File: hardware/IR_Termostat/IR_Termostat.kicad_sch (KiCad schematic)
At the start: 7 parts, among them J1 USB_C_Receptacle_PowerOnly_6P, J2 Conn_01x02_Socket, Q1 PMOS, U1 TP4056-42-ESOP8

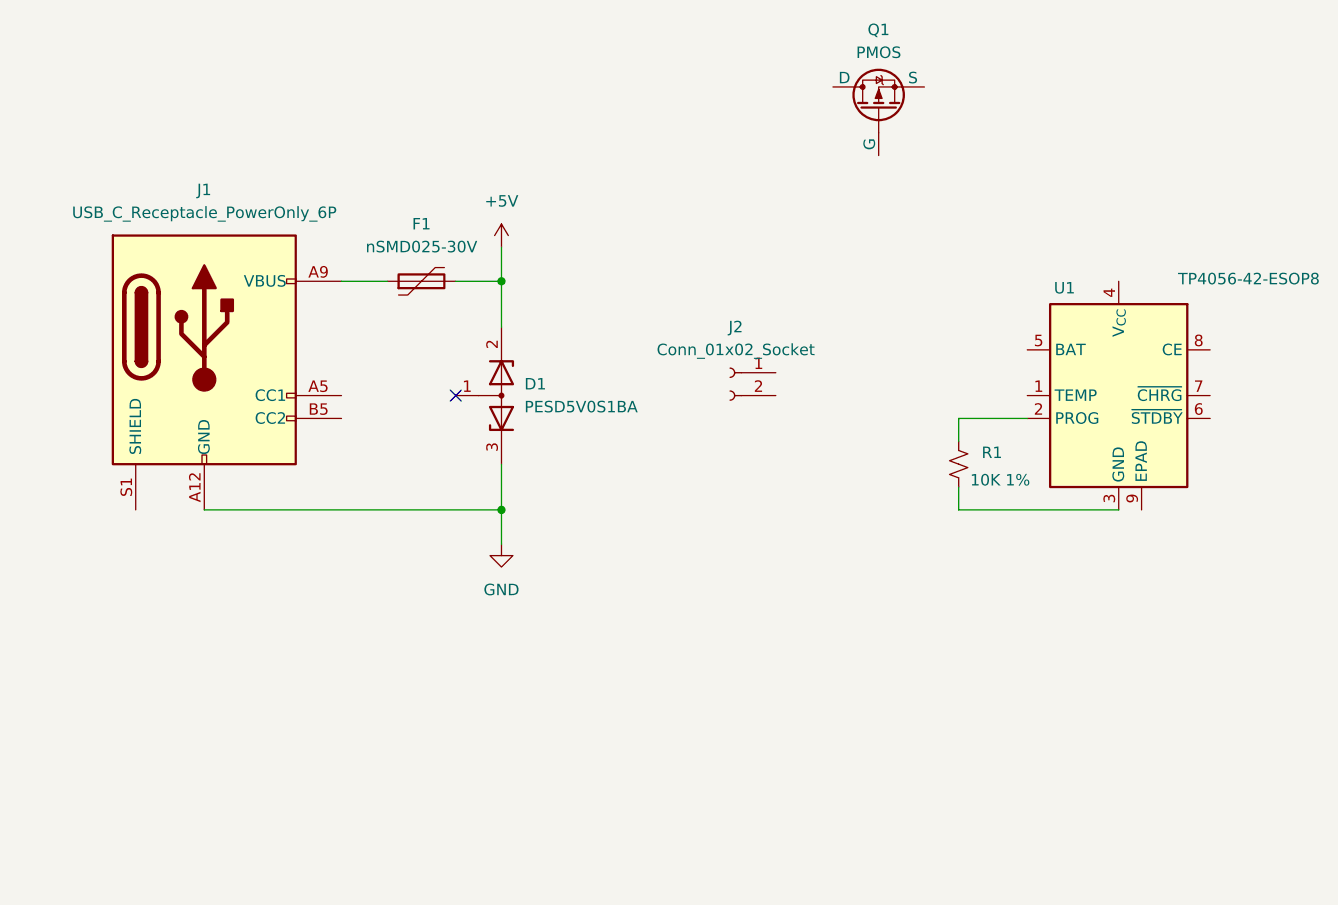
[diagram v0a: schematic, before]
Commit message: Feat: NTC improved
Also added CC1 and CC2 Resistors and a text box explaining the eletrical tolerances
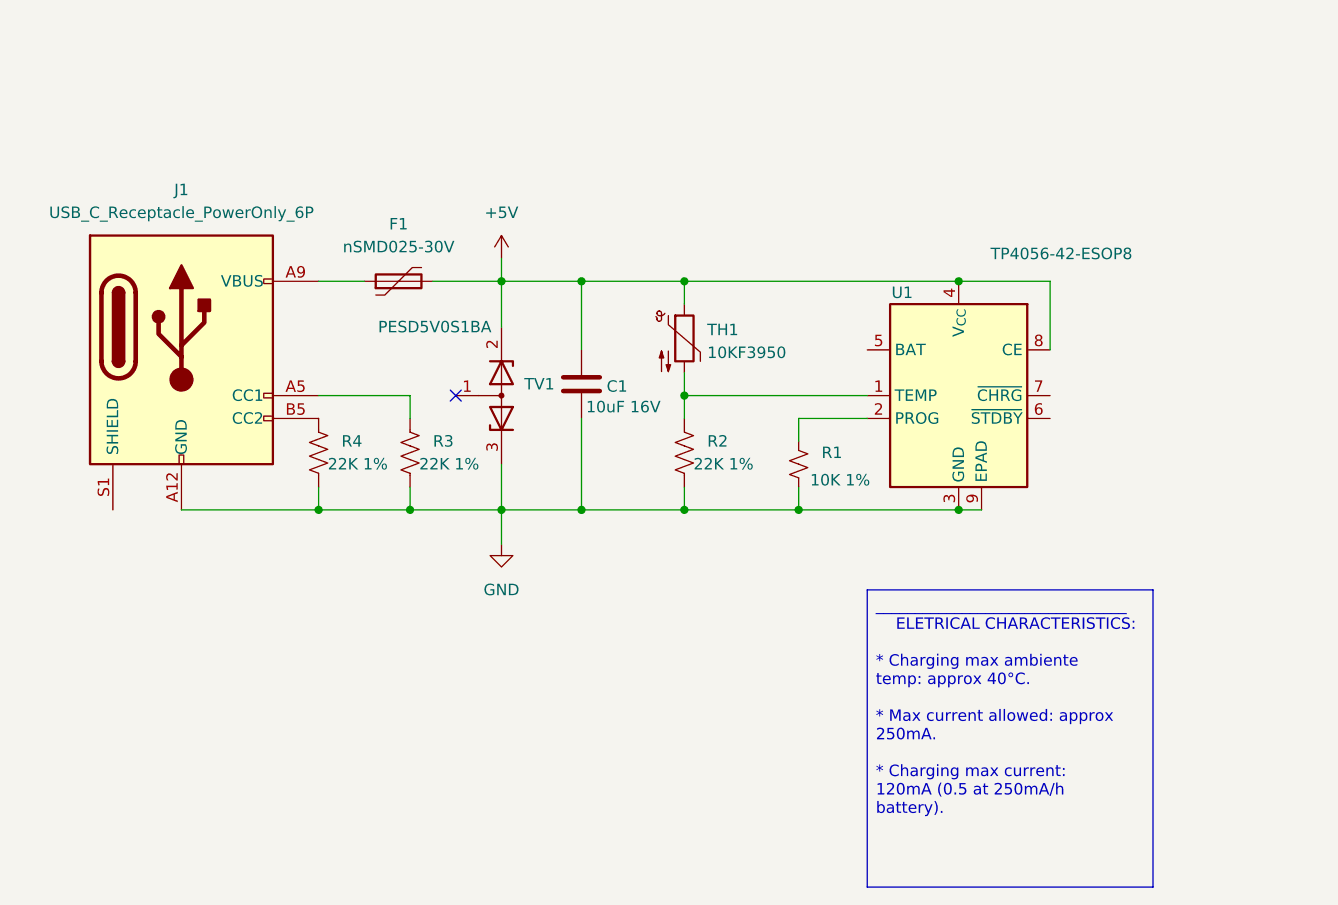
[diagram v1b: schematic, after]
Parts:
- removed J2: Conn_01x02_Socket, Connector:JWT_A3963_1x02_P3.96mm_Vertical, symbol Connector:Conn_01x02_Socket
- removed Q1: PMOS, symbol Simulation_SPICE:PMOS
- added C1: 10uF 16V, Capacitor_SMD:C_0805_2012Metric_Pad1.18x1.45mm_HandSolder, symbol Device:C
- added R2, R3, R4: 22K 1%, Resistor_SMD:R_0805_2012Metric_Pad1.20x1.40mm_HandSolder, symbol Device:R_US
- added TH1: 10KF3950, Resistor_SMD:R_0805_2012Metric_Pad1.20x1.40mm_HandSolder, symbol Device:Thermistor_NTC
- renumbered D1 to TV1
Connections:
- net +5V: now also U1.4 (V_{CC}), U1.8 (CE), C1.1, TH1.1
- net GND: now also R1.2, U1.3 (GND), U1.9 (EPAD), C1.2, R2.2, R3.2, R4.2
- net at U1.1 (TEMP): now also R2.1, TH1.2
- net at J1.A5 (CC1): now also R3.1
- net at J1.B5 (CC2): now also R4.1
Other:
- moved on the sheet: F1, J1, R1, U1

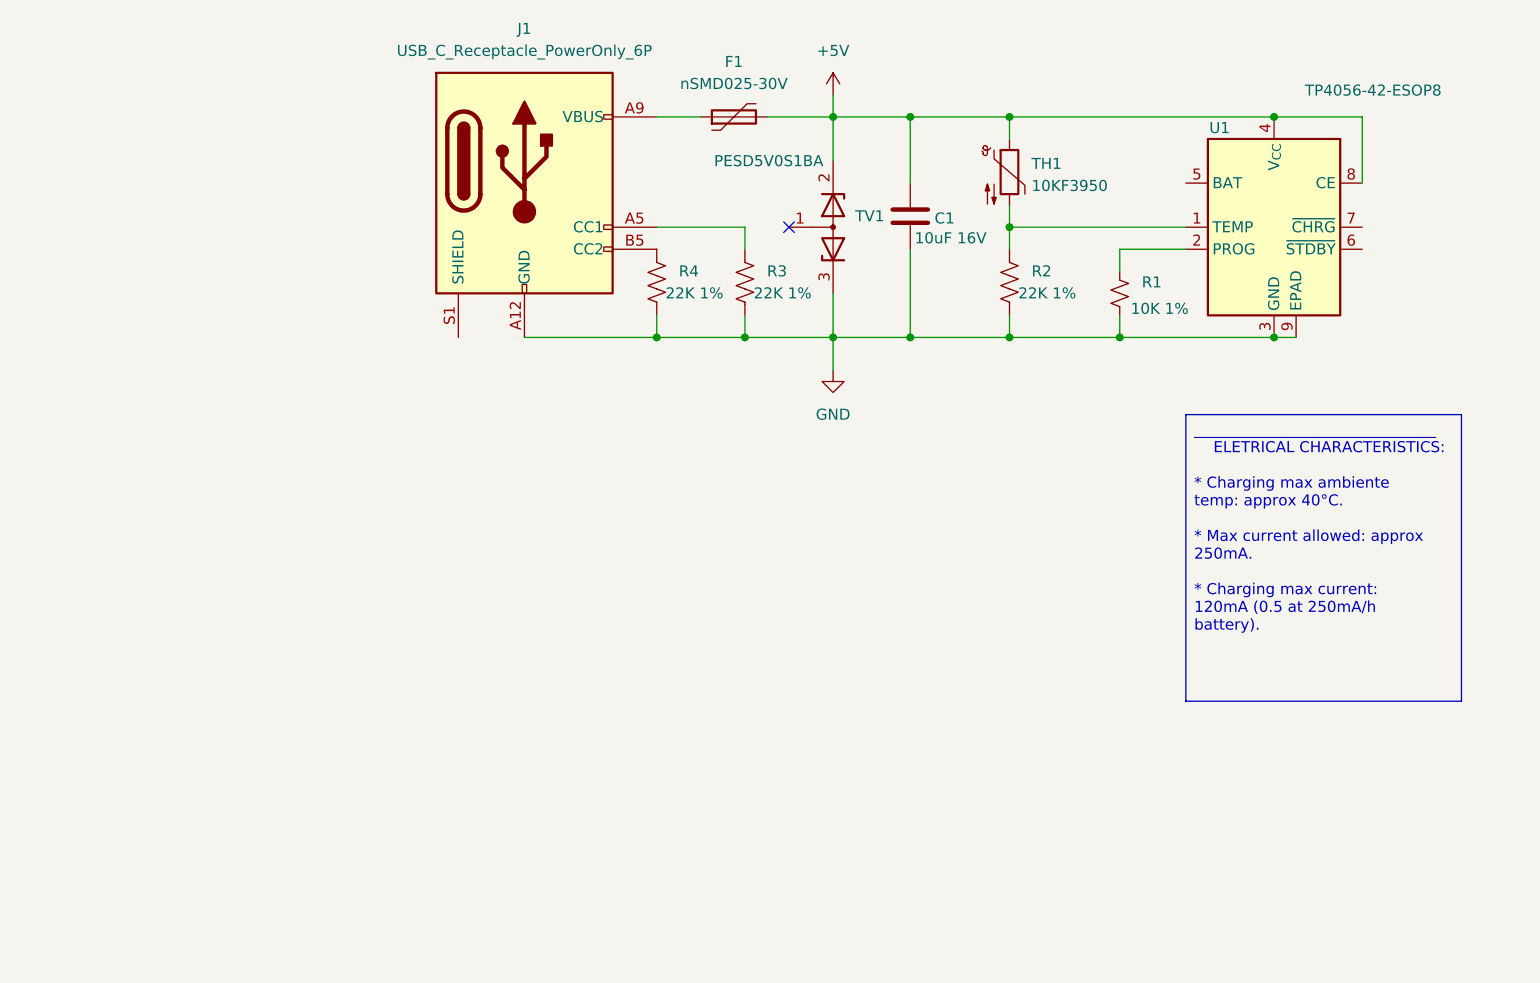
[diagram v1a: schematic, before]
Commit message: Style: Schematic refactored by sectors
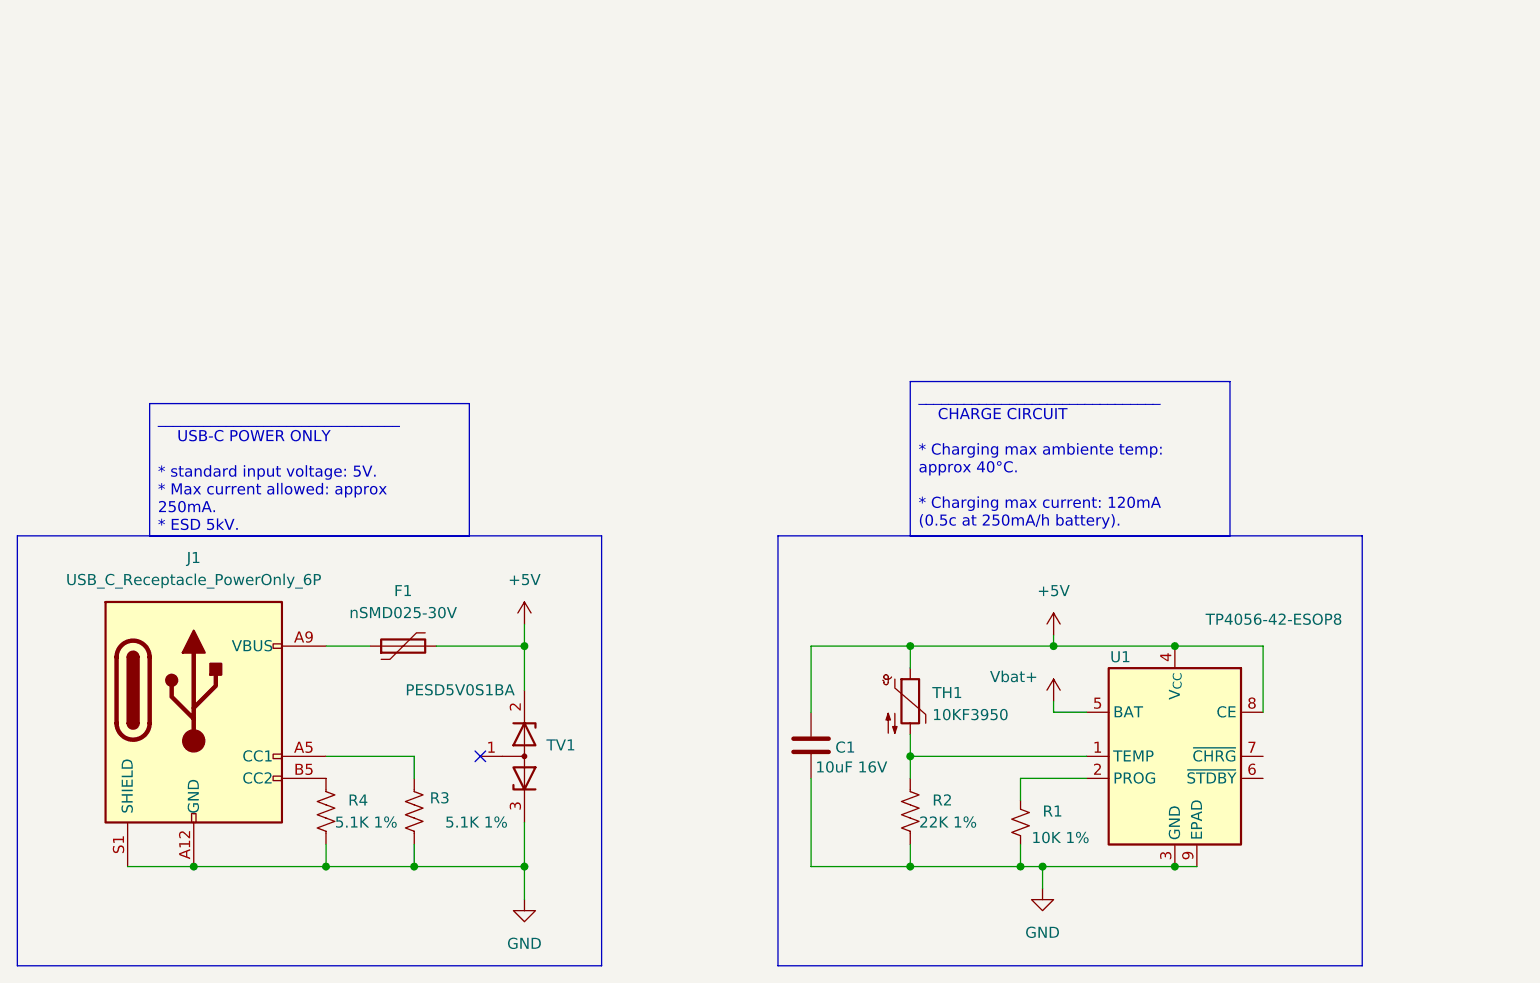
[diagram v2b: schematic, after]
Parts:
- R3, R4: value 22K 1% -> 5.1K 1%
- TV1: footprint Package_TO_SOT_SMD:SOT-323_SC-70_Handsoldering -> (none)
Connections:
- net GND: now also J1.S1 (SHIELD)
- net Vbat+: now reaches U1.5 (BAT)
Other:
- company: (none) -> Author: Lucas Oliveira.
- title: (none) -> IR termostat
- moved on the sheet: C1, F1, J1, R1, R2, R3, R4, TH1, TV1, U1

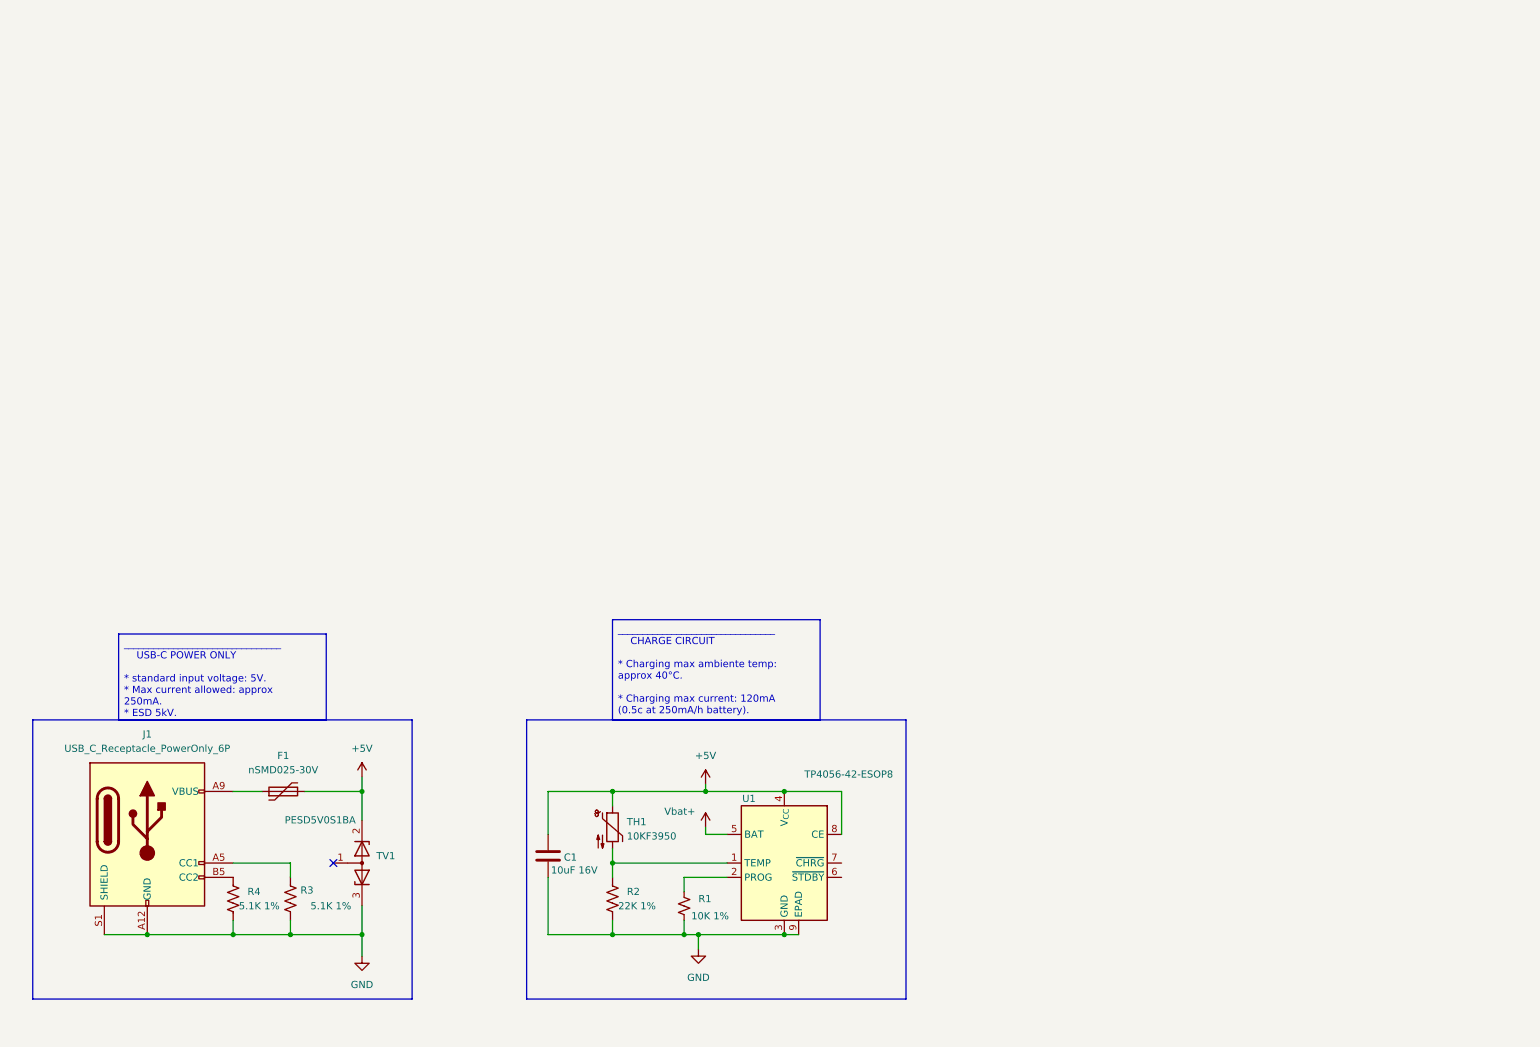
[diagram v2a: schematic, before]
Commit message: Feat: Power path with LDO implemented
Using high efficiency componentes to minimize the voltage drop-out and heat sink, for allowed levels
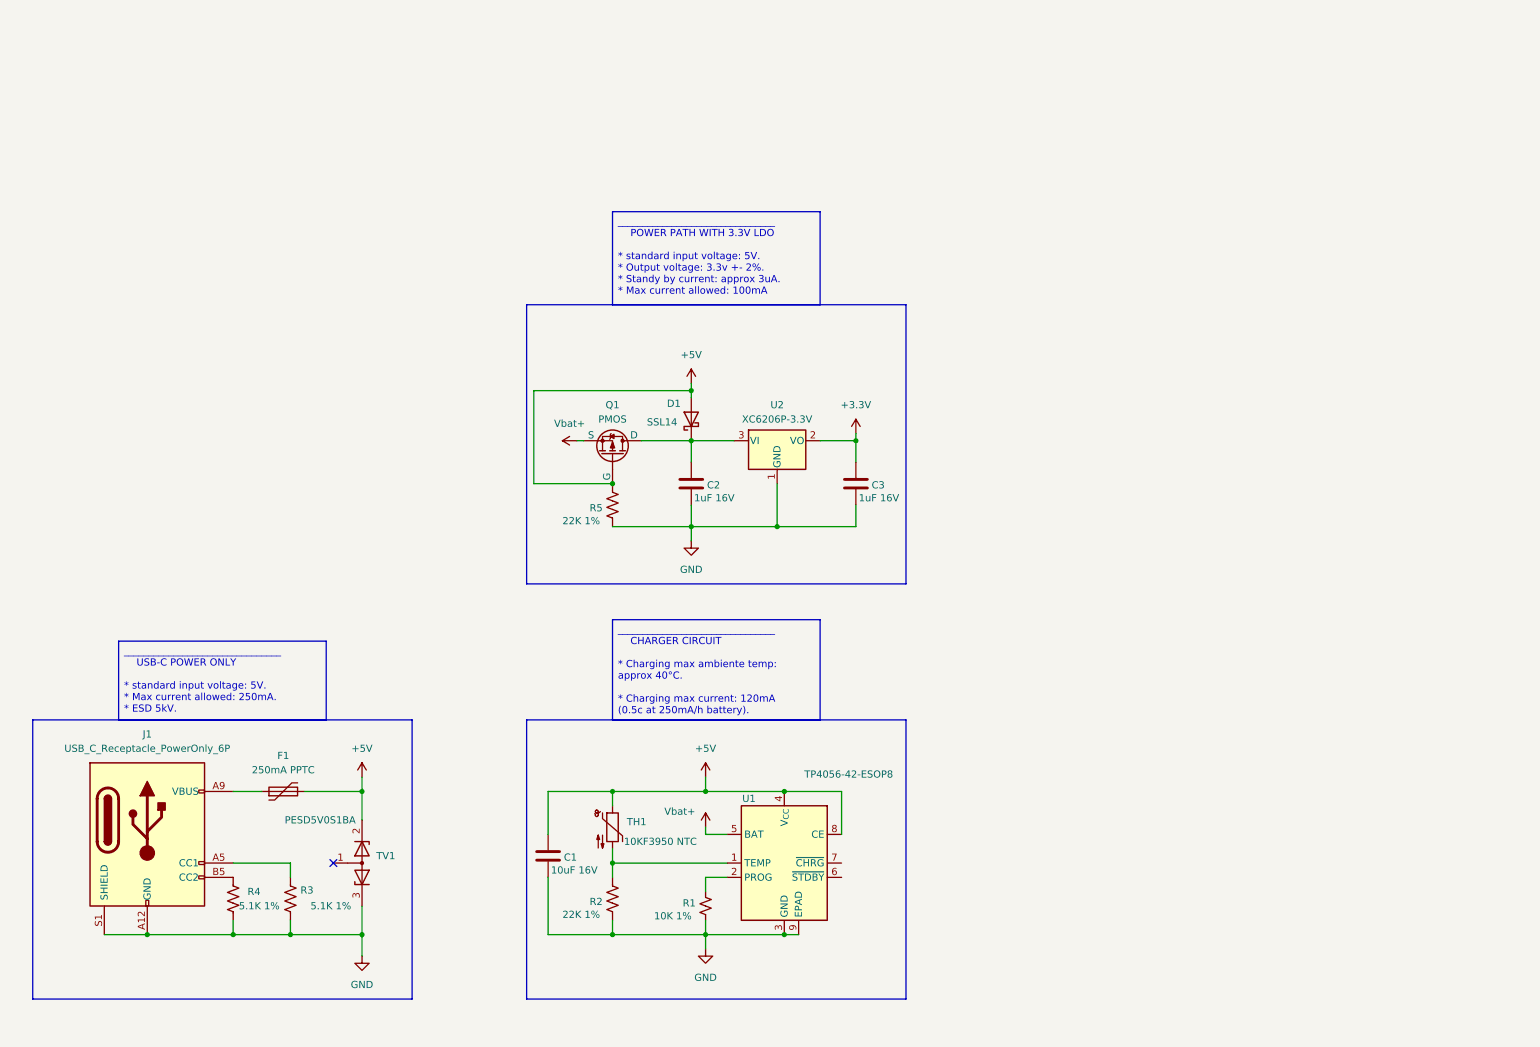
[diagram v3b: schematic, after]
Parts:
- added C2, C3: 1uF 16V, Capacitor_SMD:C_0805_2012Metric_Pad1.18x1.45mm_HandSolder, symbol Device:C
- added D1: SSL14, Diode_SMD:D_SMA_Handsoldering, symbol Diode:SS14
- added Q1: PMOS, Package_TO_SOT_SMD:SOT-23_Handsoldering, symbol Simulation_SPICE:PMOS
- added R5: 22K 1%, Resistor_SMD:R_0805_2012Metric_Pad1.20x1.40mm_HandSolder, symbol Device:R_US
- added U2: XC6206P-3.3V, Package_TO_SOT_SMD:SOT-23-3, symbol Regulator_Linear:XC6206PxxxMR
- F1: value nSMD025-30V -> 250mA PPTC
- TH1: value 10KF3950 -> 10KF3950 NTC
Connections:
- net +5V: now also D1.2 (A), Q1.2 (G), R5.1
- net GND: now also C2.2, C3.2, R5.2, U2.1 (GND)
- net Vbat+: now also Q1.3 (S)
- new net: C2.1, D1.1 (K), Q1.1 (D), U2.3 (VI)
- new net +3.3V: C3.1, U2.2 (VO)
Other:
- moved on the sheet: R1
